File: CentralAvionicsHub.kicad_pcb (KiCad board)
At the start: 2 copper layers, 106.4 x 87.9 mm, 22 parts, among them J1 GPS/ARINC, J2 MFD, J3 PFD, J4 NavCom, J5 Airframe, J6 GND1, J7 GND2, J8 Power_In, J9 Switches_Indicators

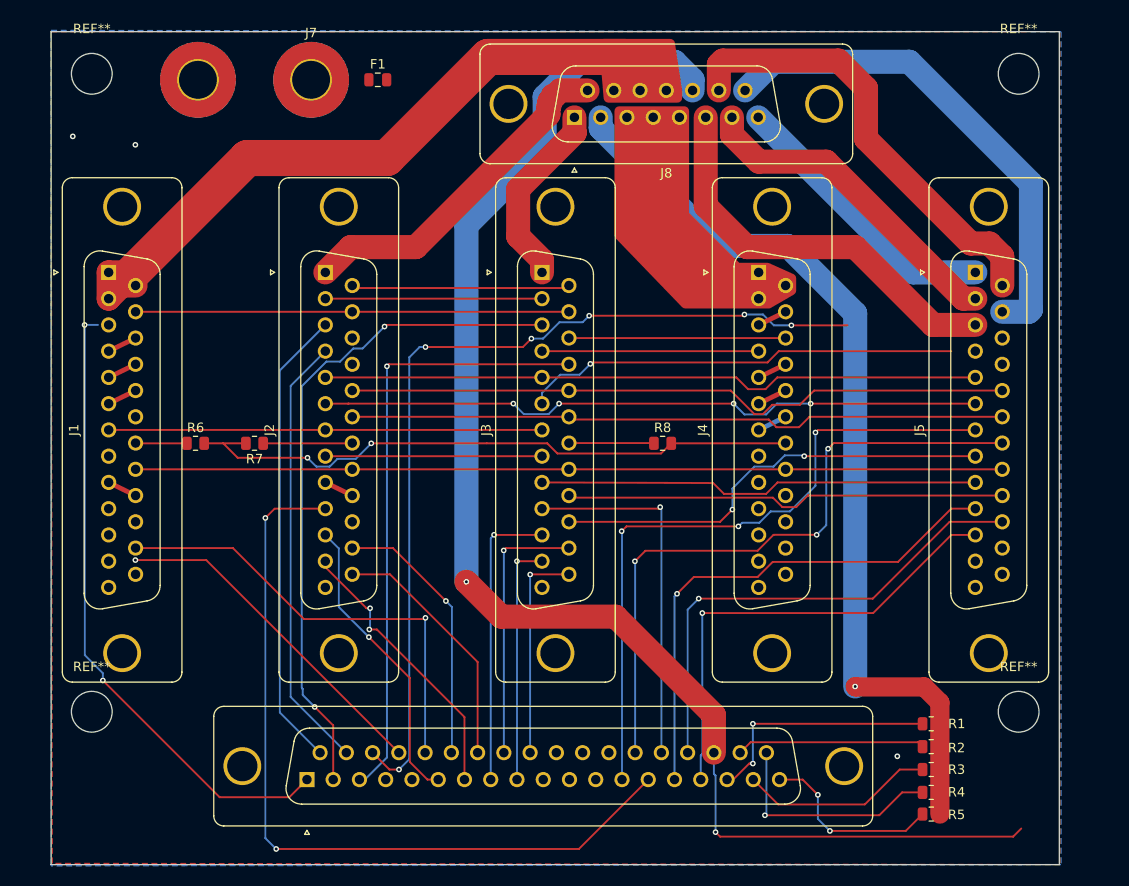
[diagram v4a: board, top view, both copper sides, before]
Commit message: Refined layout. Still need to address gnd connector
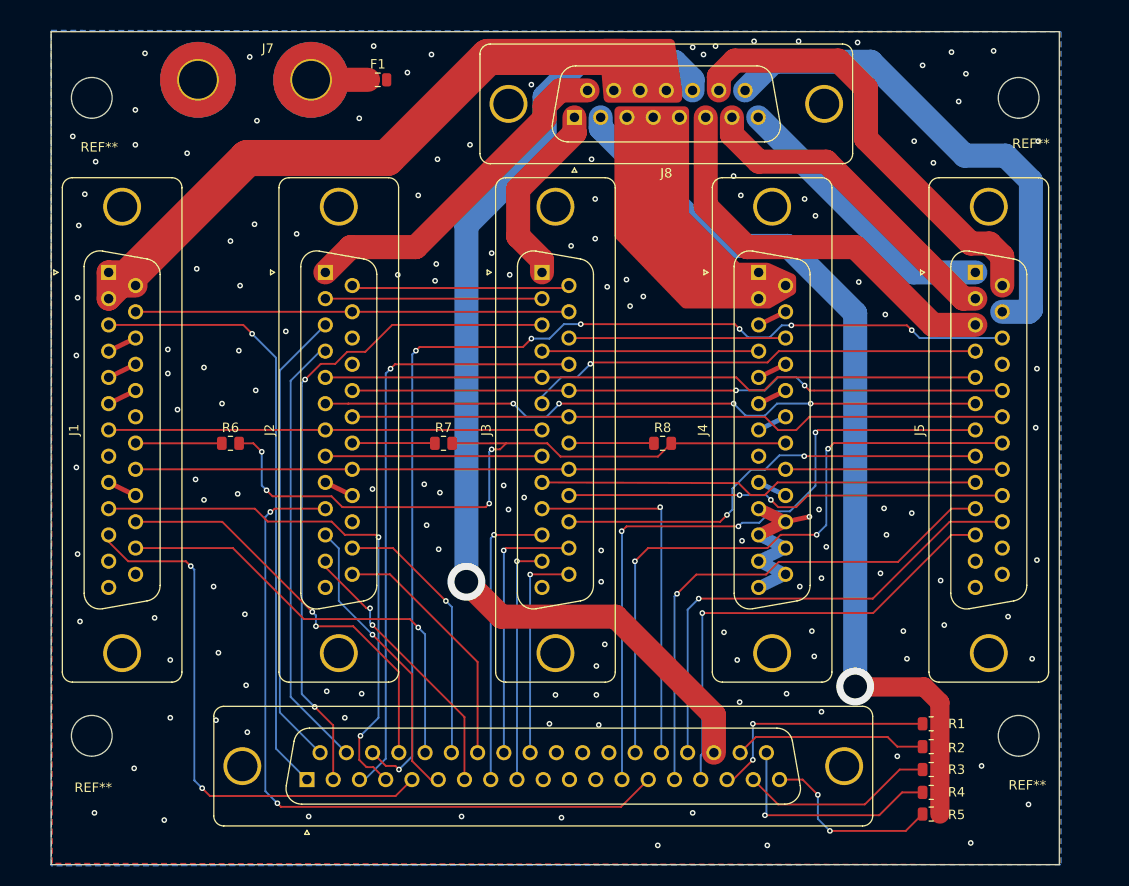
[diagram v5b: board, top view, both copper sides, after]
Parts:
- moved R7 19.9 mm to (138.0, 104.4), turned to 0 degrees
- moved R6 3.68 mm to (115.6, 104.4)
- moved REF** 2.54 mm to (100.9, 67.9)
- moved REF** 2.54 mm to (198.7, 67.9)
- moved REF** 2.54 mm to (100.9, 135.3)
- moved REF** 2.54 mm to (198.7, 135.3)
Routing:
- net /GPS_AUX1: track 0.00 -> 57.7 mm, vias 0 -> 2
- net /GPS_AUX3: track 0.00 -> 57.6 mm, vias 0 -> 2
- net Net-(J8-P13): track 150.8 -> 109.6 mm, vias 2 -> 1
- net GND: track 0.00 -> 21.5 mm, vias 3 -> 139
- net /AP_Serial_RX: track 96.1 -> 113.1 mm, vias 6 -> 7
- net /Aux_Audio: track 66.7 -> 75.4 mm, vias 2 -> 4
- net /GPS_AUX2: track 36.2 -> 43.5 mm, vias 1 -> 2
- net /MFD_Light: track 84.4 -> 77.9 mm
- net Net-(J7-Pin_1): track 0.00 -> 6.01 mm
- net /GPS_Audio: track 5.43 -> 9.11 mm
- net Net-(J4-P22): track 0.50 -> 3.66 mm
- net /EIS_Serial_RX: track 46.1 -> 48.5 mm
- net /ARINC_Serial_RX: track 67.1 -> 65.0 mm, vias 2 -> 1
- net /GPS_AUX4: track 48.0 -> 46.8 mm
- net (no net): track 1.08 -> 0.00 mm
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
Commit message: Minor Fixes, silkscreen updates.
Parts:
- J8 - POWER: renamed from J8
- renumbered J1 to J1-GPS, J2 to J2-MFD, J3 to J3-PFD, J4 to J4-NavCom, J5 to J5-Airframe, J9 to J9-Switches
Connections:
- net Net-(J1-P14) renamed /GPS_V+
- net Net-(J3-Pad1) renamed /PFD_V+
- net Net-(J4-P14) renamed /NavCom_V+
- net Net-(J5-P14) renamed /Pitch_Servo_V+
- net Net-(J5-P15) renamed /AF_Spare_V+_2
- net Net-(J5-Pad1) renamed /Roll_Servo_V+
- net Net-(J5-Pad2) renamed /AF_Spare_V+_1
- net Net-(J5-Pad3) renamed /AF_Spare_V+_3
- net Net-(J8-P13) renamed /Spare_Switchpanel_V+
- net Net-(J8-P9) renamed /MFD_V+
- net Net-(J8-Pad2) renamed /Annunciator_V+
- J2-MFD pad 16: /NavCom_SerialTX -> /NavCom_Serial_TX
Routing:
- net /NavCom_Serial_TX: track 22.9 -> 45.7 mm
- net /Annunciator_V+: track 106.4 -> 115.1 mm
- net /ARINC_Serial_RX_2: track 71.1 -> 73.2 mm
- net /Aux_Audio: track 75.4 -> 74.6 mm
- net Net-(J9-Pad37): track 24.3 -> 23.7 mm
- net GND: vias 139 -> 141

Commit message: Changed Ground connections to 250 FASTON tabs. Updated silkscreen. Corrected minor DRC errors.
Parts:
- added G***: LOGO, ahnerengineering:ahnerengineering_0.5, F.Cu at (105.5, 142.4)
- H1, H2, H3, H4: renamed from REF**; value MountingHole_4.3mm_M4_ISO7380 -> MountingHole
- J6, J7: footprint MountingHole:MountingHole_4mm_Pad_TopBottom -> FASTON_TAB:63824
- J8: renamed from J8 - POWER
- moved H1 0.13 mm to (100.9, 68.1)
- moved H2 0.13 mm to (198.7, 68.1)
- moved H3 0.13 mm to (100.9, 135.4)
- moved H4 0.13 mm to (198.7, 135.4)
- moved J9 0.13 mm to (123.6, 140.0)
- moved R2 0.13 mm to (189.5, 136.5)
- moved R4 0.13 mm to (189.5, 141.4)
- moved R5 0.13 mm to (189.5, 143.6)
- moved F1 0.13 mm to (131.1, 66.2)
- moved J1 0.13 mm to (102.7, 86.5)
- moved J2 0.13 mm to (125.6, 86.5)
- moved J3 0.13 mm to (148.4, 86.5)
- moved J4 0.13 mm to (171.3, 86.5)
- moved J5 0.13 mm to (194.2, 86.5)
- moved J6 0.13 mm to (112.1, 66.2)
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- renumbered J1-GPS to J1, J2-MFD to J2, J3-PFD to J3, J4-NavCom to J4, J5-Airframe to J5, J9-Switches to J9
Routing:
- net Net-(J7-Pin_1): track 6.01 -> 8.55 mm
- net /MZ30_Enable: track 71.3 -> 70.7 mm
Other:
- board text added: "Central Avionics Hub Rev 0: 23 November 2025"
